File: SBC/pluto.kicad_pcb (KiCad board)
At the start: 4 copper layers, 114.3 x 120.9 mm, 62 parts, among them J1 VCC1, J10 GND3, J11 Expansion Bus, J12 VIA2PB, J2 GND1, J3 VCC2, J4 POWER, J5 GND2, J6 RS232a, J7 RS232b, J9 VCC3, P1 IDE0, Q1 DS1813, SW1 RESET, SW2 PANIC, U1 WD65C02PLCC44, U2 AT28HC256EPLCC32, U22 MAX238, U23 SC28L92PLCC44, U3 IS61C256AL-12JLI, U4 DS1511Y+, U5 TL7705B, U6 PlutoDecoder, U7 WD65C22PLCC44, U8 74HC74, U9 WD65C22PLCC44, X1 8MHz, X2 3.6864MHz

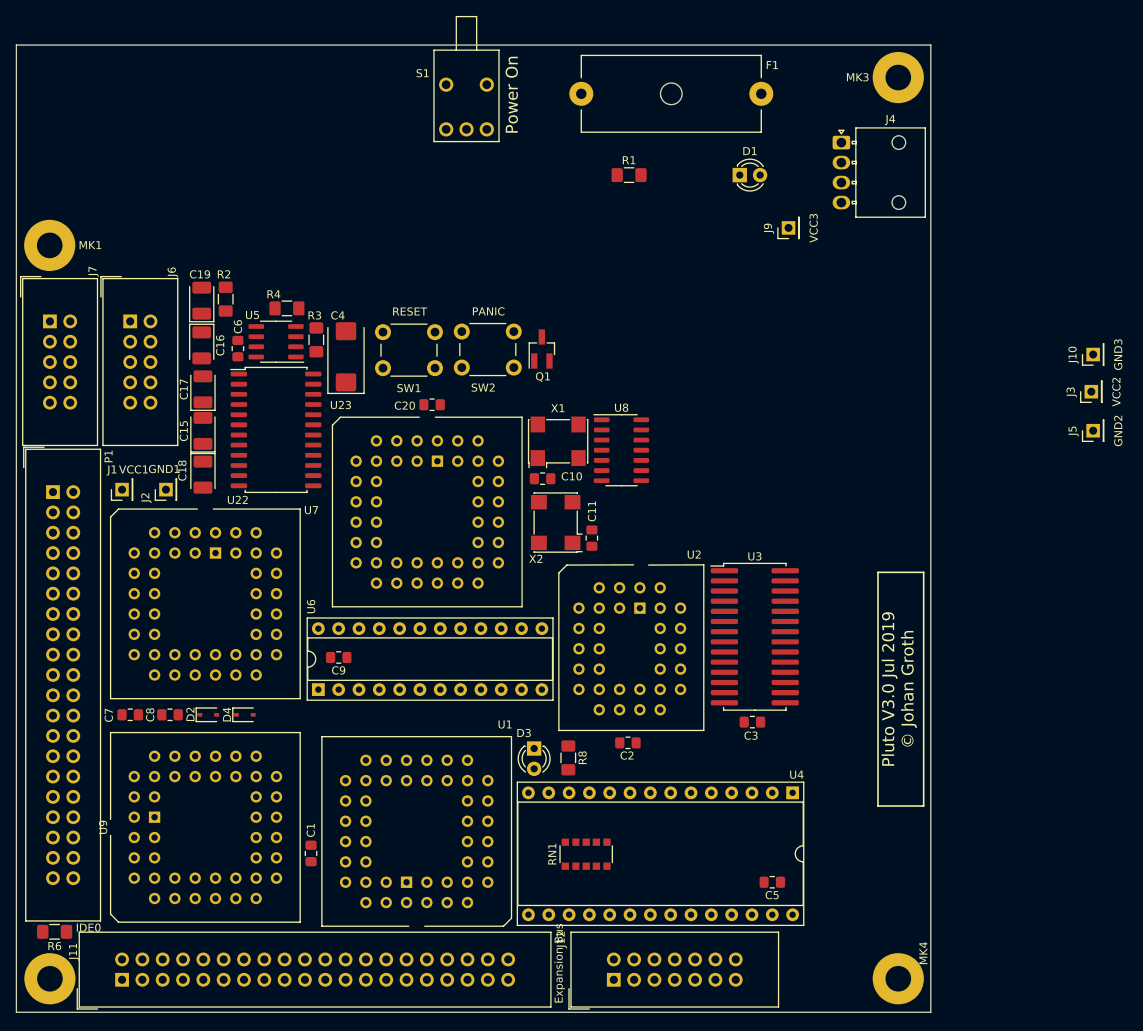
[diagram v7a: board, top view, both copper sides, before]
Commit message: Layout of PCB continues.
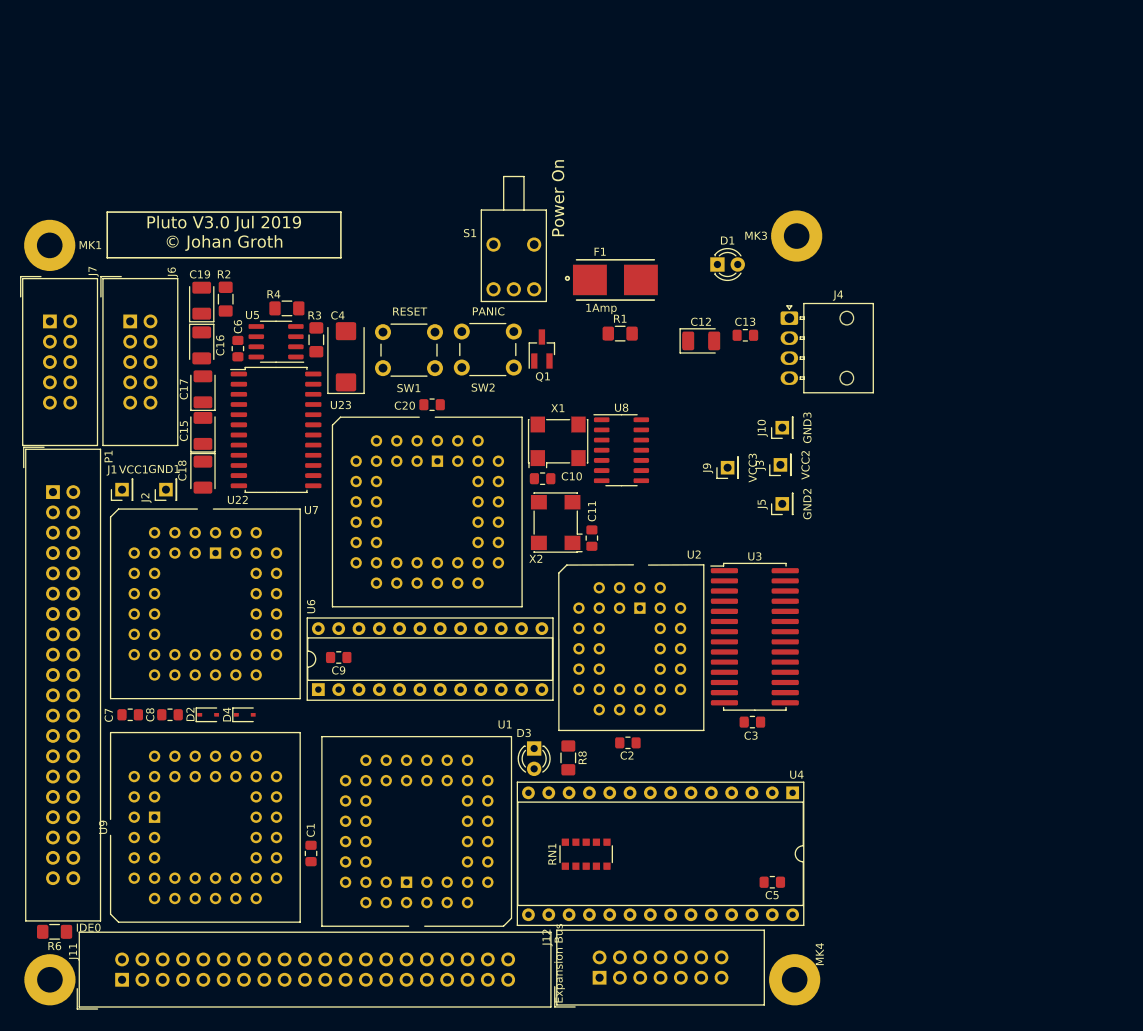
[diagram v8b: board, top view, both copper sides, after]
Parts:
- added C12: 100uF, Capacitor_Tantalum_SMD:CP_EIA-3528-15_AVX-H_Pad1.50x2.35mm_HandSolder, F.Cu at (139.8, 56.8)
- added C13: 0.1uF, Capacitor_SMD:C_0805_2012Metric_Pad1.15x1.40mm_HandSolder, F.Cu at (145.3, 56.1)
- F1: footprint Fuse:Fuseholder_Cylinder-5x20mm_Schurter_0031_8201_Horizontal_Open -> Grotto:FUSE_0154004.DR
- R1: value 1kOhm -> 1k
- moved J5 39.9 mm to (150.0, 77.2)
- moved J10 39.9 mm to (150.0, 67.6)
- moved J3 39.9 mm to (149.7, 72.3)
- moved J9 30.9 mm to (143.1, 72.6)
- moved F1 23.7 mm to (129.1, 49.2)
- moved MK3 23.5 mm to (151.8, 43.7)
- moved J4 22.9 mm to (150.9, 53.9)
- moved S1 20.8 mm to (116.4, 47.3)
- moved R1 19.8 mm to (129.7, 55.9)
- moved MK4 13.0 mm to (151.5, 136.7)
- moved D1 11.5 mm to (141.9, 47.2)
- moved J12 1.80 mm to (127.1, 136.4)
- moved MK6 0.13 mm to (58.4, 136.7)
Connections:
- D1 pad 1: Net-(D1-Pad1) -> GND
- D1 pad 2: VCC -> Net-(D1-Pad2)
- R1 pad 1: GND -> VCC
- R1 pad 2: Net-(D1-Pad1) -> Net-(D1-Pad2)
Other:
- board outline removed
